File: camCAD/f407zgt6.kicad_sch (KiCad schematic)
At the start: 2 parts, among them J2 SWD Header, U3 STM32F407ZGTx

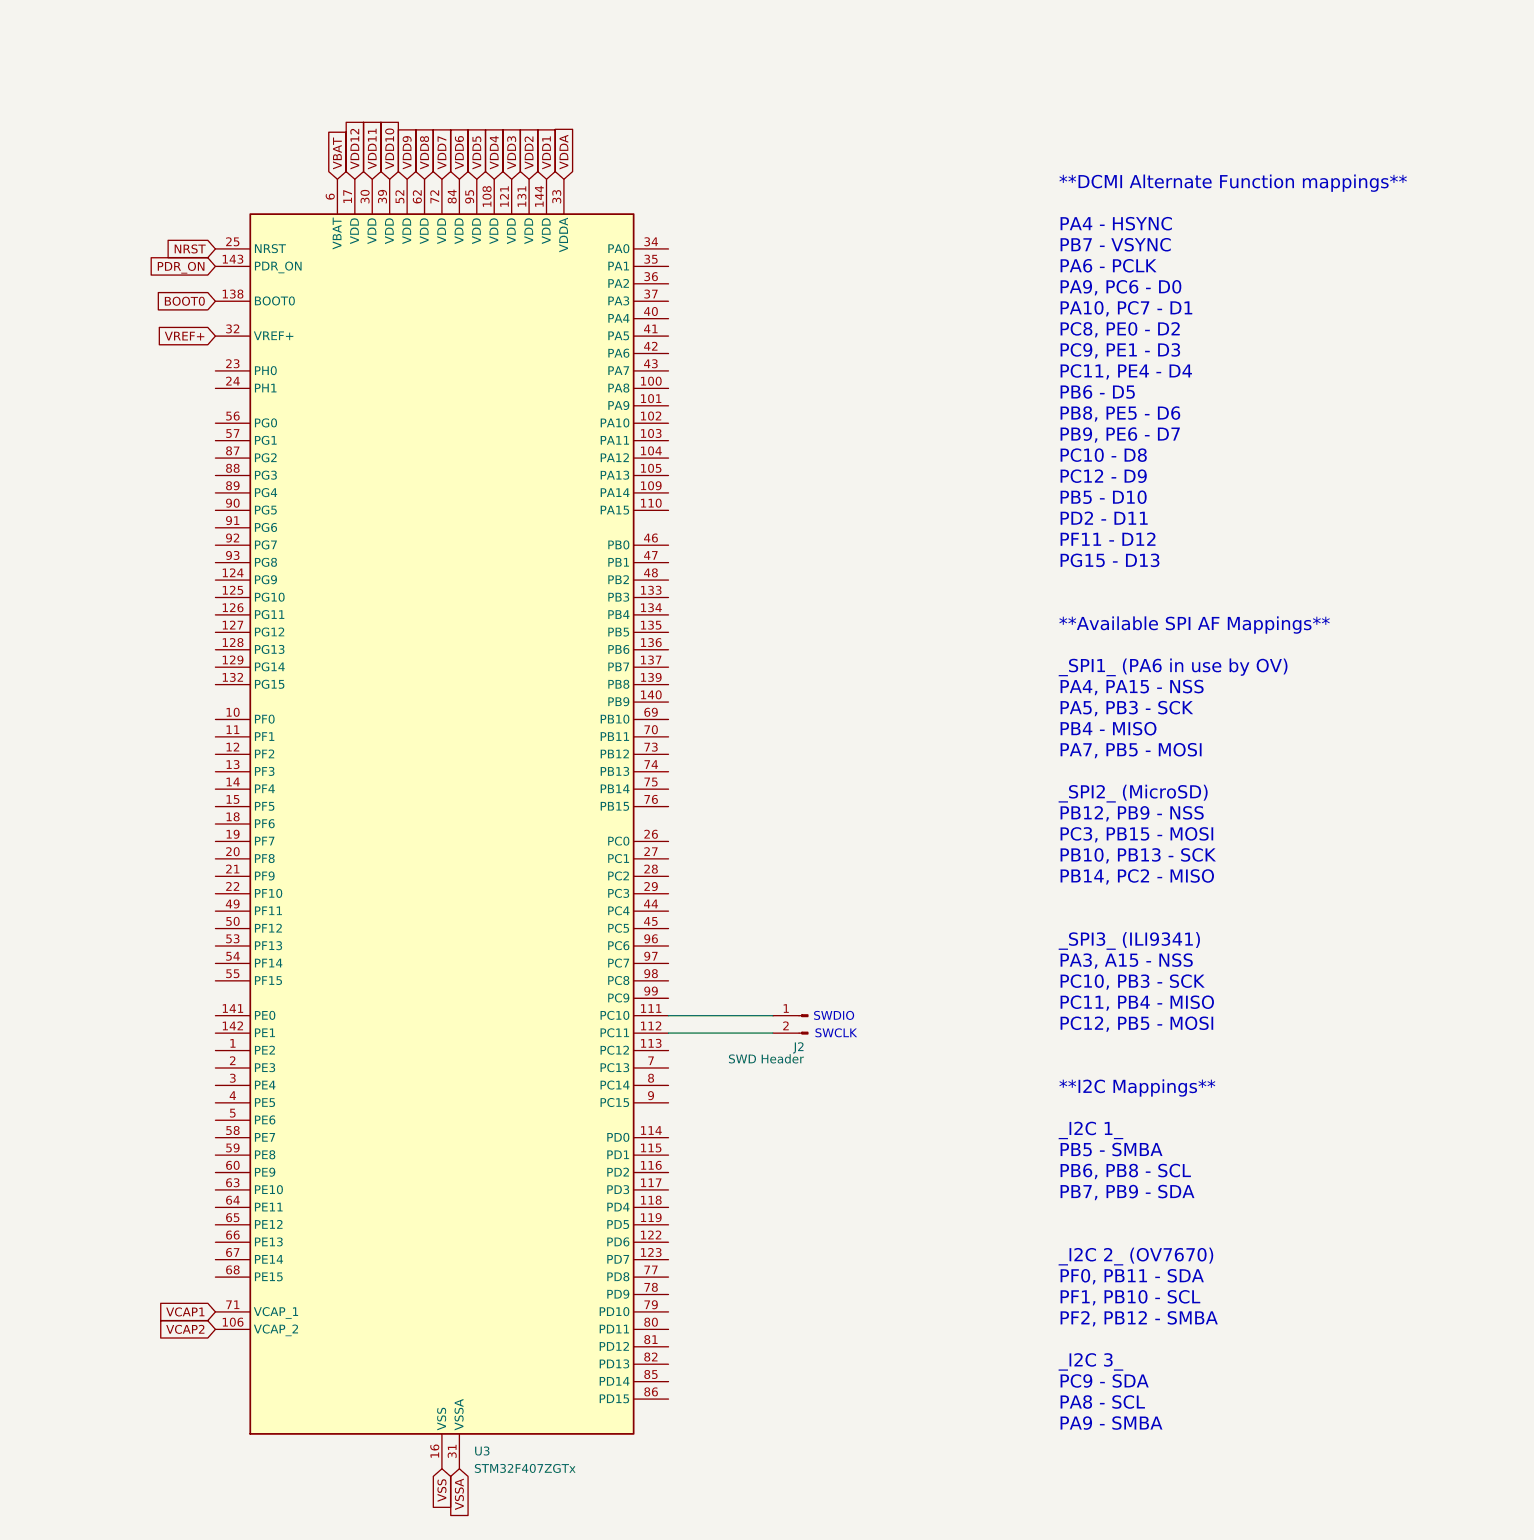
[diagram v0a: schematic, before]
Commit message: Added battery to HardwareNotes.md, some touch ups on schematic
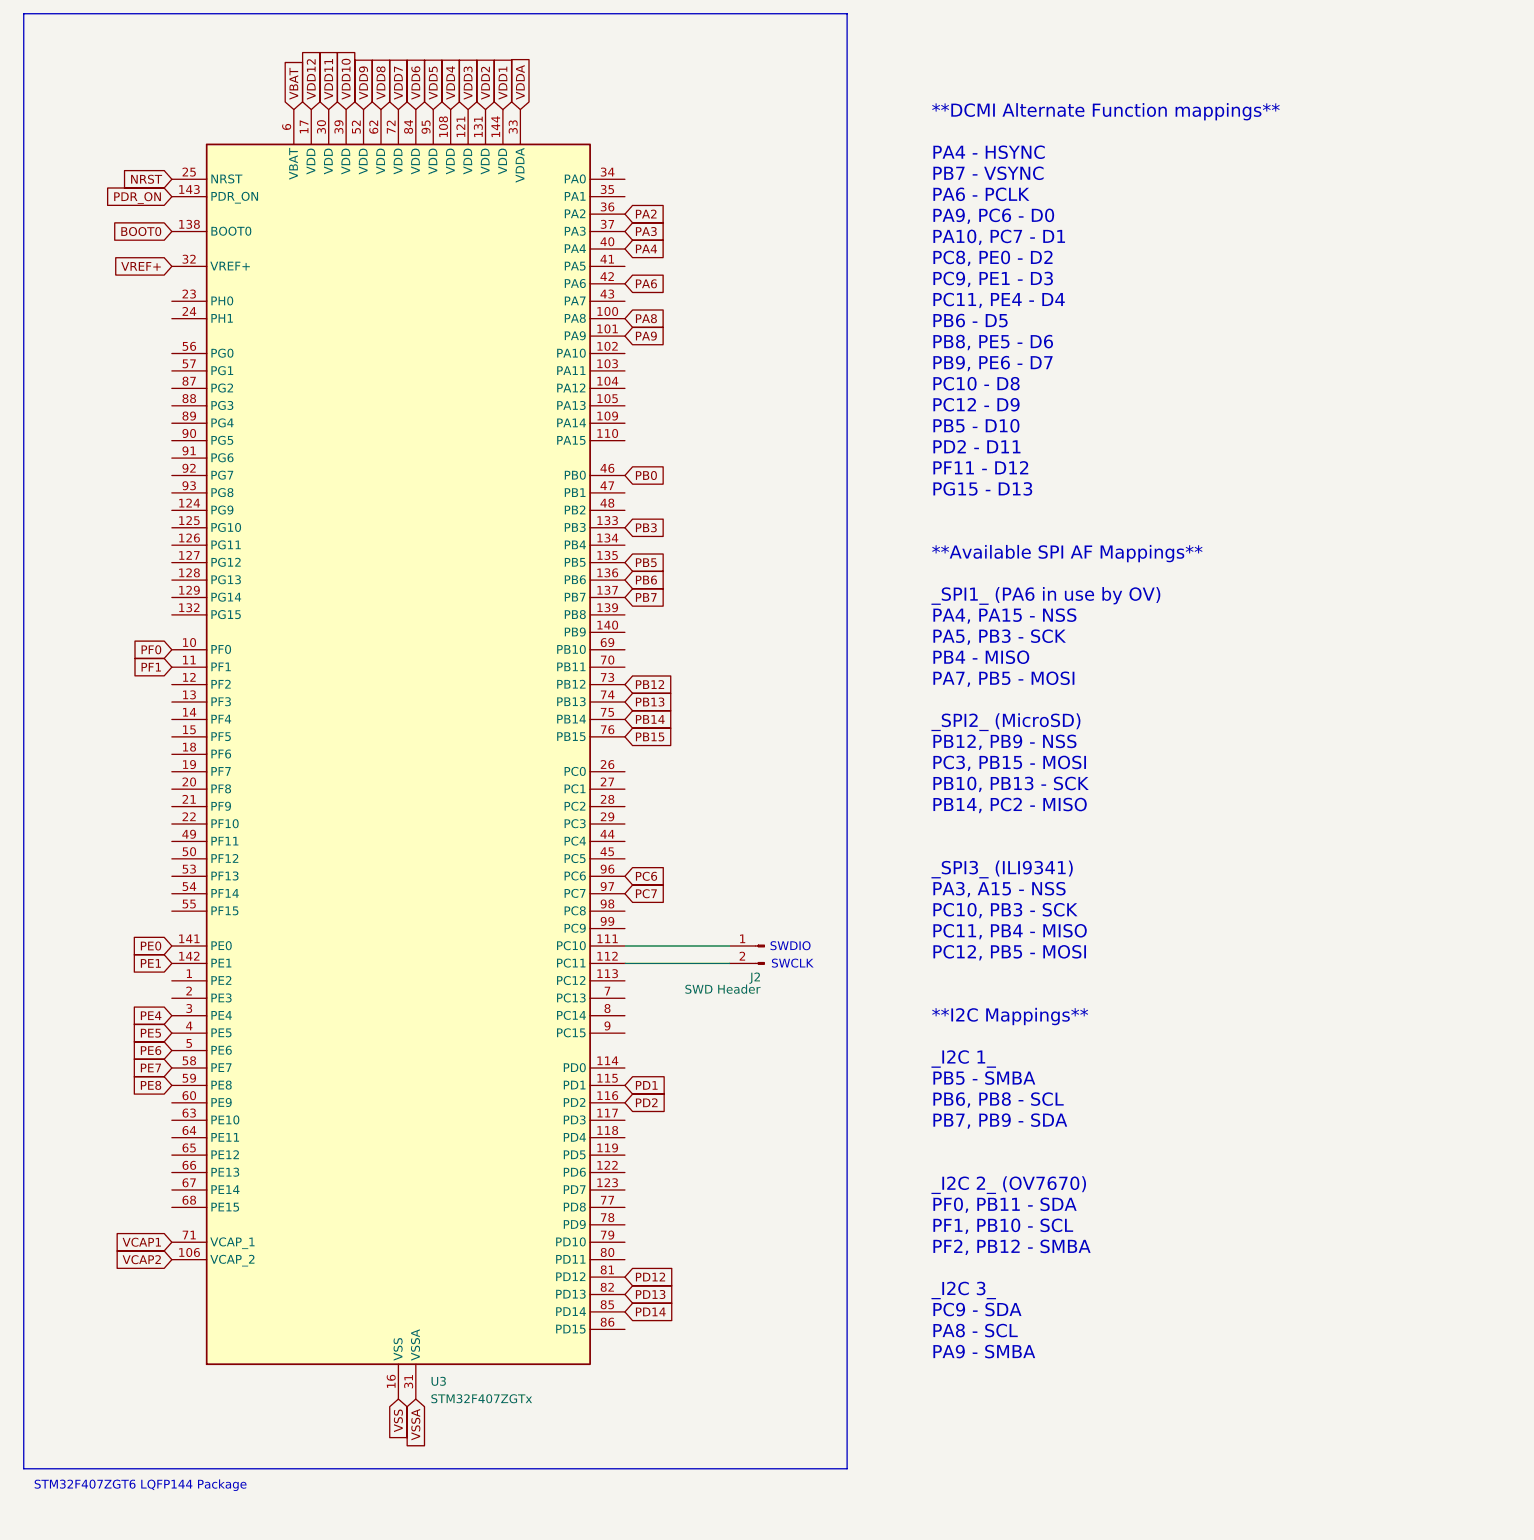
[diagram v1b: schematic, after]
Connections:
- net PF0: now reaches U3.10 (PF0)
- net PA8: now reaches U3.100 (PA8)
- net PA9: now reaches U3.101 (PA9)
- net PF1: now reaches U3.11 (PF1)
- net PD1: now reaches U3.115 (PD1)
- net PD2: now reaches U3.116 (PD2)
- net PB3: now reaches U3.133 (PB3)
- net PB5: now reaches U3.135 (PB5)
- net PB6: now reaches U3.136 (PB6)
- net PB7: now reaches U3.137 (PB7)
- net PE0: now reaches U3.141 (PE0)
- net PE1: now reaches U3.142 (PE1)
- net PE4: now reaches U3.3 (PE4)
- net PA2: now reaches U3.36 (PA2)
- net PA3: now reaches U3.37 (PA3)
- net PE5: now reaches U3.4 (PE5)
- net PA4: now reaches U3.40 (PA4)
- net PA6: now reaches U3.42 (PA6)
- net PB0: now reaches U3.46 (PB0)
- net PE6: now reaches U3.5 (PE6)
- net PE7: now reaches U3.58 (PE7)
- net PE8: now reaches U3.59 (PE8)
- net PB12: now reaches U3.73 (PB12)
- net PB13: now reaches U3.74 (PB13)
- net PB14: now reaches U3.75 (PB14)
- net PB15: now reaches U3.76 (PB15)
- net PD12: now reaches U3.81 (PD12)
- net PD13: now reaches U3.82 (PD13)
- net PD14: now reaches U3.85 (PD14)
- net PC6: now reaches U3.96 (PC6)
- net PC7: now reaches U3.97 (PC7)
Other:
- note added: "STM32F407ZGT6 LQFP144 Package"
- title: (none) -> STM32F407ZGT6 Pinout 
- moved on the sheet: J2, U3
